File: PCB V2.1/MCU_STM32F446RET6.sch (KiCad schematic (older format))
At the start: 35 parts, among them J1 20021121-00010C4LF, J2 0475890001-MicroUSBPort, SW1 B3U-1000P, U1 STM32F446RET6_-_TQFP64, X1 ABM3B8.000MHZB2T, X2 ABS07-32.768KHZ-9-T

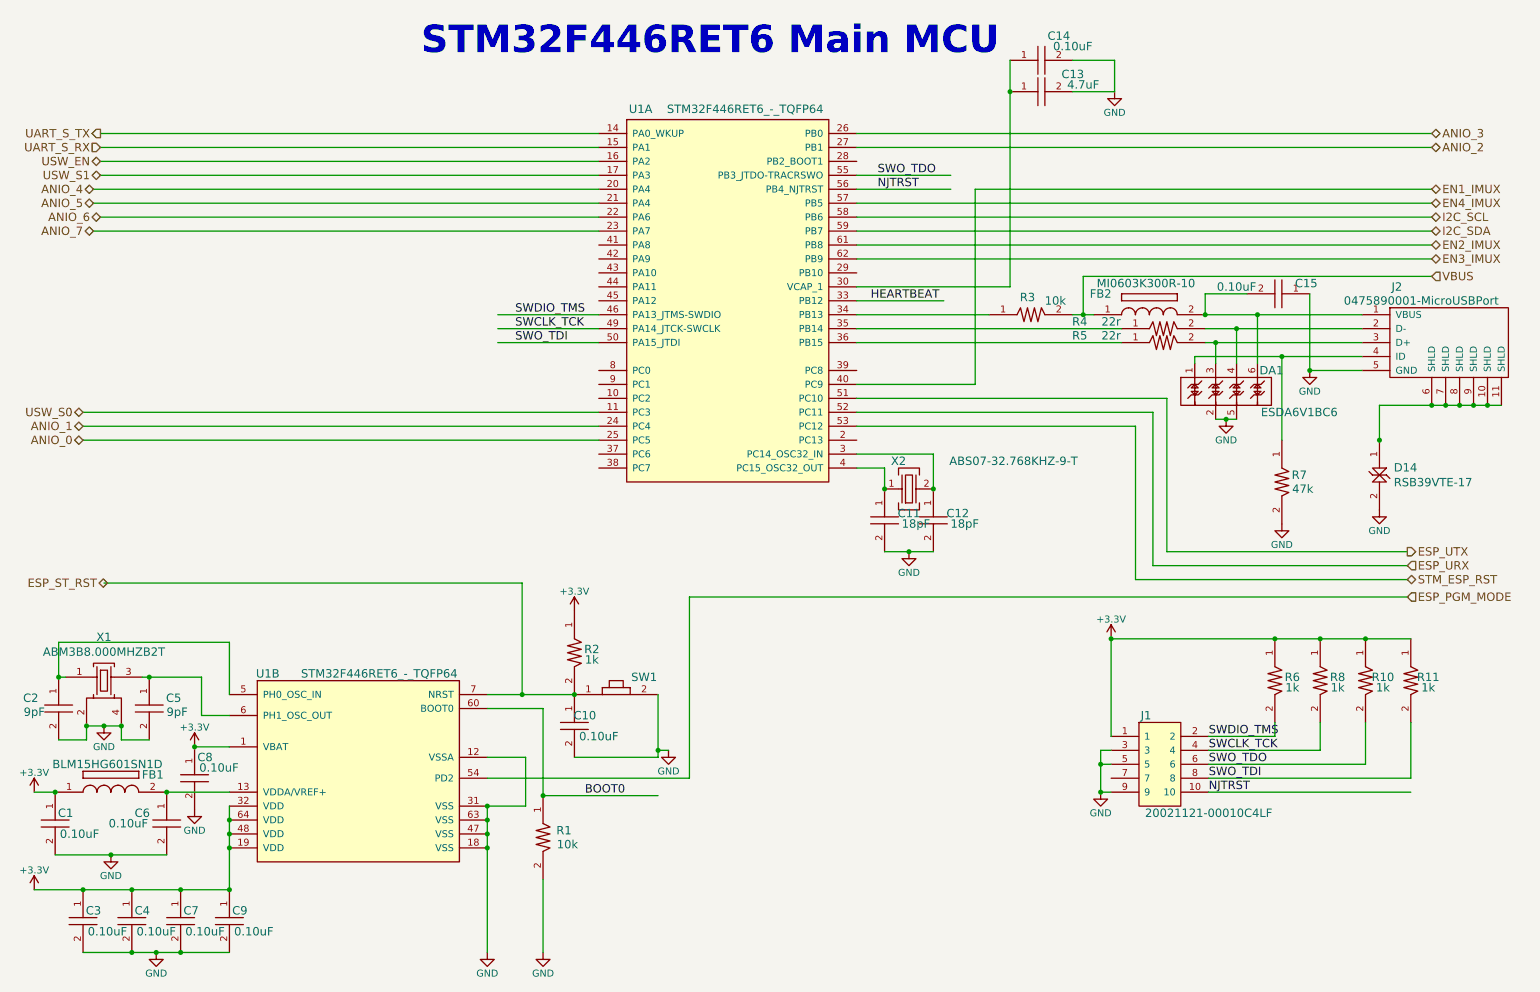
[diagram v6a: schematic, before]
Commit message: OTA
This commit contains adjustments to the schematics for over the air
update/programming of STM32 via the ESP8266 using its internal
bootloader. The two processors have been wired together to suppor this
fucntions, they can toggle reset of eachother and load firmware over
UART. Still deciding what reset signal pin on the STM32 to use fo rthis
purpose, next commit.
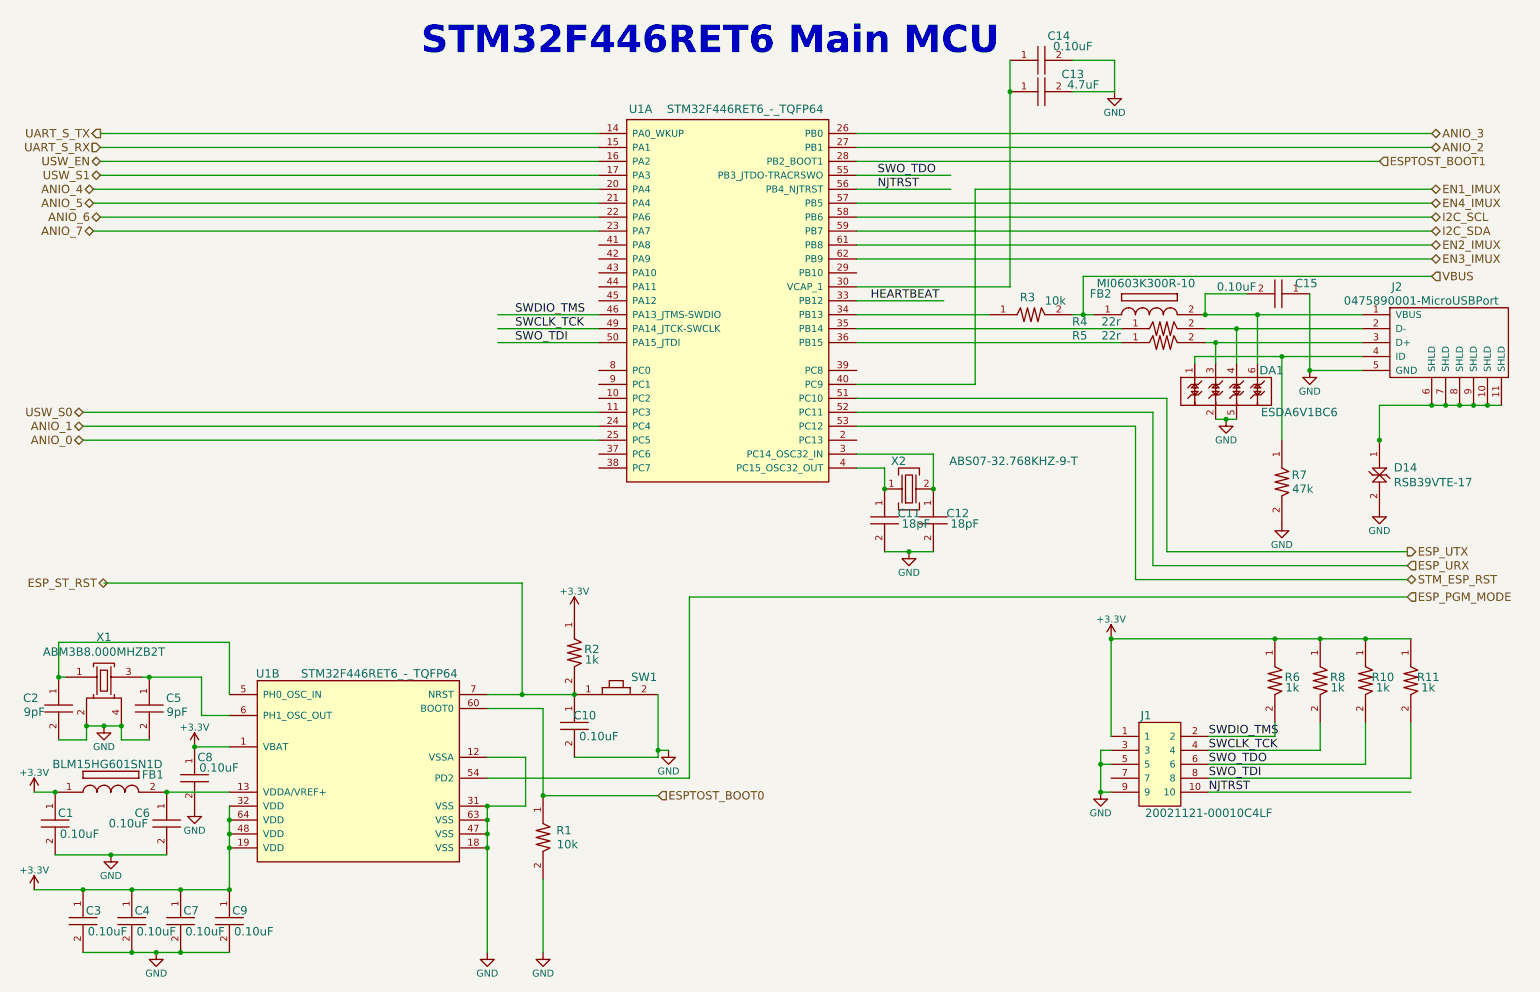
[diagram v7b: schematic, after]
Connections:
- net labels added: ESPTOST_BOOT0, ESPTOST_BOOT1
- net labels removed: BOOT0
- wire segments 119 -> 120
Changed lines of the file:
@@
 LIBS:HydroPWNics_Lib
 LIBS:ESP32-footprints-Shem-Lib
+LIBS:ESP8266
 LIBS:SunLeaf_V2-cache
 EELAYER 25 0
@@
 $EndComp
 $Comp
-L GND #PWR4
+L GND #PWR01
 U 1 1 57D43B63
 P 1125 6625
-F 0 "#PWR4" H 1125 6375 50  0001 C CNN
+F 0 "#PWR01" H 1125 6375 50  0001 C CNN
 F 1 "GND" H 1125 6475 50  0000 C CNN
 F 2 "" H 1125 6625 50  0000 C CNN
@@
 $EndComp
 $Comp
-L GND #PWR5
+L GND #PWR02
 U 1 1 57D43E04
 P 1450 7325
-F 0 "#PWR5" H 1450 7075 50  0001 C CNN
+F 0 "#PWR02" H 1450 7075 50  0001 C CNN
 F 1 "GND" H 1450 7175 50  0000 C CNN
 F 2 "" H 1450 7325 50  0000 C CNN
@@
 $EndComp
 $Comp
-L +3.3V #PWR1
+L +3.3V #PWR03
 U 1 1 57D443BB
 P 575 6175
-F 0 "#PWR1" H 575 6025 50  0001 C CNN
+F 0 "#PWR03" H 575 6025 50  0001 C CNN
 F 1 "+3.3V" H 575 6315 50  0000 C CNN
 F 2 "" H 575 6175 50  0000 C CNN
@@
 $EndComp
 $Comp
-L +3.3V #PWR2
+L +3.3V #PWR04
 U 1 1 57D444DD
 P 575 6875
-F 0 "#PWR2" H 575 6725 50  0001 C CNN
+F 0 "#PWR04" H 575 6725 50  0001 C CNN
 F 1 "+3.3V" H 575 7015 50  0000 C CNN
 F 2 "" H 575 6875 50  0000 C CNN
@@
 $EndComp
 $Comp
-L GND #PWR11
+L GND #PWR05
 U 1 1 57D449FF
 P 5125 5875
-F 0 "#PWR11" H 5125 5625 50  0001 C CNN
+F 0 "#PWR05" H 5125 5625 50  0001 C CNN
 F 1 "GND" H 5125 5725 50  0000 C CNN
 F 2 "" H 5125 5875 50  0000 C CNN
@@
 $EndComp
 $Comp
-L +3.3V #PWR10
+L +3.3V #PWR06
 U 1 1 57D45F91
 P 4450 4875
-F 0 "#PWR10" H 4450 4725 50  0001 C CNN
+F 0 "#PWR06" H 4450 4725 50  0001 C CNN
 F 1 "+3.3V" H 4450 5015 50  0000 C CNN
 F 2 "" H 4450 4875 50  0000 C CNN
@@
 $EndComp
 $Comp
-L GND #PWR8
+L GND #PWR07
 U 1 1 57D46AC6
 P 3825 7325
-F 0 "#PWR8" H 3825 7075 50  0001 C CNN
+F 0 "#PWR07" H 3825 7075 50  0001 C CNN
 F 1 "GND" H 3825 7175 50  0000 C CNN
 F 2 "" H 3825 7325 50  0000 C CNN
@@
 $EndComp
 $Comp
-L GND #PWR9
+L GND #PWR08
 U 1 1 57D47BC2
 P 4225 7325
-F 0 "#PWR9" H 4225 7075 50  0001 C CNN
+F 0 "#PWR08" H 4225 7075 50  0001 C CNN
 F 1 "GND" H 4225 7175 50  0000 C CNN
 F 2 "" H 4225 7325 50  0000 C CNN
@@
 	1    0    0    -1
 $EndComp
-Text Label 4525 6200 0    60   ~ 0
-BOOT0
 $Comp
 L CL05C090CB5NNNC C2
@@
 $EndComp
 $Comp
-L GND #PWR3
+L GND #PWR09
 U 1 1 57D49635
 P 1075 5700
-F 0 "#PWR3" H 1075 5450 50  0001 C CNN
+F 0 "#PWR09" H 1075 5450 50  0001 C CNN
 F 1 "GND" H 1075 5550 50  0000 C CNN
 F 2 "" H 1075 5700 50  0000 C CNN
@@
 $EndComp
 $Comp
-L GND #PWR12
+L GND #PWR010
 U 1 1 57D4B2EA
 P 6850 4450
-F 0 "#PWR12" H 6850 4200 50  0001 C CNN
+F 0 "#PWR010" H 6850 4200 50  0001 C CNN
 F 1 "GND" H 6850 4300 50  0000 C CNN
 F 2 "" H 6850 4450 50  0000 C CNN
@@
 $EndComp
 $Comp
-L GND #PWR7
+L GND #PWR011
 U 1 1 57D4C07E
 P 1725 6300
-F 0 "#PWR7" H 1725 6050 50  0001 C CNN
+F 0 "#PWR011" H 1725 6050 50  0001 C CNN
 F 1 "GND" H 1725 6150 50  0000 C CNN
 F 2 "" H 1725 6300 50  0000 C CNN
@@
 $EndComp
 $Comp
-L GND #PWR14
+L GND #PWR012
 U 1 1 57D53F54
 P 8325 1150
-F 0 "#PWR14" H 8325 900 50  0001 C CNN
+F 0 "#PWR012" H 8325 900 50  0001 C CNN
 F 1 "GND" H 8325 1000 50  0000 C CNN
 F 2 "" H 8325 1150 50  0000 C CNN
@@
 $EndComp
 $Comp
-L GND #PWR18
+L GND #PWR013
 U 1 1 57D5C6D5
 P 10225 4150
-F 0 "#PWR18" H 10225 3900 50  0001 C CNN
+F 0 "#PWR013" H 10225 3900 50  0001 C CNN
 F 1 "GND" H 10225 4000 50  0000 C CNN
 F 2 "" H 10225 4150 50  0000 C CNN
@@
 $EndComp
 $Comp
-L GND #PWR16
+L GND #PWR014
 U 1 1 57D5C856
 P 9525 4250
-F 0 "#PWR16" H 9525 4000 50  0001 C CNN
+F 0 "#PWR014" H 9525 4000 50  0001 C CNN
 F 1 "GND" H 9525 4100 50  0000 C CNN
 F 2 "" H 9525 4250 50  0000 C CNN
@@
 $EndComp
 $Comp
-L GND #PWR17
+L GND #PWR015
 U 1 1 57D5C8C7
 P 9725 3150
-F 0 "#PWR17" H 9725 2900 50  0001 C CNN
+F 0 "#PWR015" H 9725 2900 50  0001 C CNN
 F 1 "GND" H 9725 3000 50  0000 C CNN
 F 2 "" H 9725 3150 50  0000 C CNN
@@
 $EndComp
 $Comp
-L GND #PWR15
+L GND #PWR016
 U 1 1 57D5FF55
 P 9125 3500
-F 0 "#PWR15" H 9125 3250 50  0001 C CNN
+F 0 "#PWR016" H 9125 3250 50  0001 C CNN
 F 1 "GND" H 9125 3350 50  0000 C CNN
 F 2 "" H 9125 3500 50  0000 C CNN
@@
 $EndComp
 $Comp
-L +3.3V #PWR13
+L +3.3V #PWR017
 U 1 1 57D61D70
 P 8300 5075
-F 0 "#PWR13" H 8300 4925 50  0001 C CNN
+F 0 "#PWR017" H 8300 4925 50  0001 C CNN
 F 1 "+3.3V" H 8300 5215 50  0000 C CNN
 F 2 "" H 8300 5075 50  0000 C CNN
@@
 Connection ~ 9725 3150
 $Comp
-L +3.3V #PWR6
+L +3.3V #PWR018
 U 1 1 57D91770
 P 1725 5850
-F 0 "#PWR6" H 1725 5700 50  0001 C CNN
+F 0 "#PWR018" H 1725 5700 50  0001 C CNN
 F 1 "+3.3V" H 1725 5990 50  0000 C CNN
 F 2 "" H 1725 5850 50  0000 C CNN
@@
 $EndComp
 $Comp
-L GND #PWR?
+L GND #PWR019
 U 1 1 57DDB978
 P 8225 6175
-F 0 "#PWR?" H 8225 5925 50  0001 C CNN
+F 0 "#PWR019" H 8225 5925 50  0001 C CNN
 F 1 "GND" H 8225 6025 50  0000 C CNN
 F 2 "" H 8225 6175 50  0000 C CNN
@@
 $EndComp
 Connection ~ 8225 6175
+Text HLabel 5050 6200 2    59   Input ~ 0
+ESPTOST_BOOT0
+Text HLabel 10225 1650 2    59   Input ~ 0
+ESPTOST_BOOT1
+Wire Wire Line
+	10225 1650 6475 1650
 $EndSCHEMATC
